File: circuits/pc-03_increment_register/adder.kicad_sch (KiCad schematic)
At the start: 9 parts, among them U10 4081, U11 4070, U12 4070, U13 4011, U5 74LS283, U6 74LS283, U7 74LS283, U8 74LS283, U9 4081

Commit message: Kicad upgrade to 9.0
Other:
- company: (none) -> Adder Circuit
- title: (none) -> PC-03 Increment Unit
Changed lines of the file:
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@@
 (kicad_sch
-	(version 20231120)
+	(version 20250114)
 	(generator "eeschema")
-	(generator_version "8.0")
+	(generator_version "9.0")
 	(paper "A4")
+	(title_block
+		(title "PC-03 Increment Unit")
+		(date "2025-02-18")
+		(rev "A")
+		(company "Adder Circuit")
+	)
 	(junction
 		(at 171.45 86.36)
@@
 	(label "reg9"
 		(at 120.65 68.58 0)
-		(fields_autoplaced yes)
 		(effects
 			(font
@@
 	(label "reg11"
 		(at 120.65 73.66 0)
-		(fields_autoplaced yes)
 		(effects
 			(font
@@
 	(label "inc14"
 		(at 196.85 66.04 0)
-		(fields_autoplaced yes)
 		(effects
 			(font
@@
 	(label "inc3"
 		(at 59.69 68.58 0)
-		(fields_autoplaced yes)
 		(effects
 			(font
@@
 	(label "inc7"
 		(at 105.41 68.58 0)
-		(fields_autoplaced yes)
 		(effects
 			(font
@@
 	(label "reg6"
 		(at 74.93 71.12 0)
-		(fields_autoplaced yes)
 		(effects
 			(font
@@
 	(label "inc15"
 		(at 196.85 68.58 0)
-		(fields_autoplaced yes)
 		(effects
 			(font
@@
 	(label "reg3"
 		(at 29.21 73.66 0)
-		(fields_autoplaced yes)
 		(effects
 			(font
@@
 	(label "reg13"
 		(at 166.37 68.58 0)
-		(fields_autoplaced yes)
 		(effects
 			(font
@@
 	(label "reg12"
 		(at 166.37 66.04 0)
-		(fields_autoplaced yes)
 		(effects
 			(font
@@
 	(label "reg4"
 		(at 74.93 66.04 0)
-		(fields_autoplaced yes)
 		(effects
 			(font
@@
 	(label "inc4"
 		(at 105.41 60.96 0)
-		(fields_autoplaced yes)
 		(effects
 			(font
@@
 	(label "reg0"
 		(at 29.21 66.04 0)
-		(fields_autoplaced yes)
 		(effects
 			(font
@@
 	(label "reg14"
 		(at 166.37 71.12 0)
-		(fields_autoplaced yes)
 		(effects
 			(font
@@
 	(label "reg1"
 		(at 29.21 68.58 0)
-		(fields_autoplaced yes)
 		(effects
 			(font
@@
 	(label "offset6"
 		(at 132.08 172.72 0)
-		(fields_autoplaced yes)
 		(effects
 			(font
@@
 	(label "inc11"
 		(at 151.13 68.58 0)
-		(fields_autoplaced yes)
 		(effects
 			(font
@@
 	(label "inc9"
 		(at 151.13 63.5 0)
-		(fields_autoplaced yes)
 		(effects
 			(font
@@
 	(label "inc10"
 		(at 151.13 66.04 0)
-		(fields_autoplaced yes)
 		(effects
 			(font
@@
 	(label "inc8"
 		(at 151.13 60.96 0)
-		(fields_autoplaced yes)
 		(effects
 			(font
@@
 	(label "inc12"
 		(at 196.85 60.96 0)
-		(fields_autoplaced yes)
 		(effects
 			(font
@@
 	(label "inc0"
 		(at 59.69 60.96 0)
-		(fields_autoplaced yes)
 		(effects
 			(font
@@
 	(label "reg5"
 		(at 74.93 68.58 0)
-		(fields_autoplaced yes)
 		(effects
 			(font
@@
 	(label "inc6"
 		(at 105.41 66.04 0)
-		(fields_autoplaced yes)
 		(effects
 			(font
@@
 	(label "reg7"
 		(at 74.93 73.66 0)
-		(fields_autoplaced yes)
 		(effects
 			(font
@@
 	(label "reg10"
 		(at 120.65 71.12 0)
-		(fields_autoplaced yes)
 		(effects
 			(font
@@
 	(label "offset3"
 		(at 82.55 172.72 0)
-		(fields_autoplaced yes)
 		(effects
 			(font
@@
 	(label "offset4"
 		(at 101.6 172.72 0)
-		(fields_autoplaced yes)
 		(effects
 			(font
@@
 	(label "offset2"
 		(at 67.31 172.72 0)
-		(fields_autoplaced yes)
 		(effects
 			(font
@@
 	(label "inc13"
 		(at 196.85 63.5 0)
-		(fields_autoplaced yes)
 		(effects
 			(font
@@
 	(label "offset1"
 		(at 52.07 172.72 0)
-		(fields_autoplaced yes)
 		(effects
 			(font
@@
 	(label "inc1"
 		(at 59.69 63.5 0)
-		(fields_autoplaced yes)
 		(effects
 			(font
@@
 	(label "offset5"
 		(at 116.84 172.72 0)
-		(fields_autoplaced yes)
 		(effects
 			(font
@@
 	(label "offset0"
 		(at 36.83 172.72 0)
-		(fields_autoplaced yes)
 		(effects
 			(font
@@
 	(label "offset7"
 		(at 147.32 172.72 0)
-		(fields_autoplaced yes)
 		(effects
 			(font
@@
 	(label "inc2"
 		(at 59.69 66.04 0)
-		(fields_autoplaced yes)
 		(effects
 			(font
@@
 	(label "carry_in"
 		(at 187.96 102.87 0)
-		(fields_autoplaced yes)
 		(effects
 			(font
@@
 	(label "reg2"
 		(at 29.21 71.12 0)
-		(fields_autoplaced yes)
 		(effects
 			(font
@@
 	(label "inc5"
 		(at 105.41 63.5 0)
-		(fields_autoplaced yes)
 		(effects
 			(font
@@
 	(label "reg8"
 		(at 120.65 66.04 0)
-		(fields_autoplaced yes)
 		(effects
 			(font
@@
 	(label "reg15"
 		(at 166.37 73.66 0)
-		(fields_autoplaced yes)
 		(effects
 			(font
@@
 		(shape output)
 		(at 204.47 52.07 90)
-		(fields_autoplaced yes)
 		(effects
 			(font
@@
 		(shape output)
 		(at 158.75 52.07 90)
-		(fields_autoplaced yes)
 		(effects
 			(font
@@
 		(shape input)
 		(at 118.11 59.69 90)
-		(fields_autoplaced yes)
 		(effects
 			(font
@@
 		(shape output)
 		(at 67.31 52.07 90)
-		(fields_autoplaced yes)
 		(effects
 			(font
@@
 		(shape input)
 		(at 72.39 59.69 90)
-		(fields_autoplaced yes)
 		(effects
 			(font
@@
 		(shape output)
 		(at 113.03 52.07 90)
-		(fields_autoplaced yes)
 		(effects
 			(font
@@
 		(shape input)
 		(at 25.4 149.86 180)
-		(fields_autoplaced yes)
 		(effects
 			(font
@@
 		(shape input)
 		(at 25.4 175.26 180)
-		(fields_autoplaced yes)
 		(effects
 			(font
@@
 		(shape input)
 		(at 163.83 59.69 90)
-		(fields_autoplaced yes)
 		(effects
 			(font
@@
 		(shape input)
 		(at 26.67 59.69 90)
-		(fields_autoplaced yes)
 		(effects
 			(font
@@
 		(shape input)
 		(at 25.4 170.18 180)
-		(fields_autoplaced yes)
-		(effects
-			(font
+		(effects
+			(font

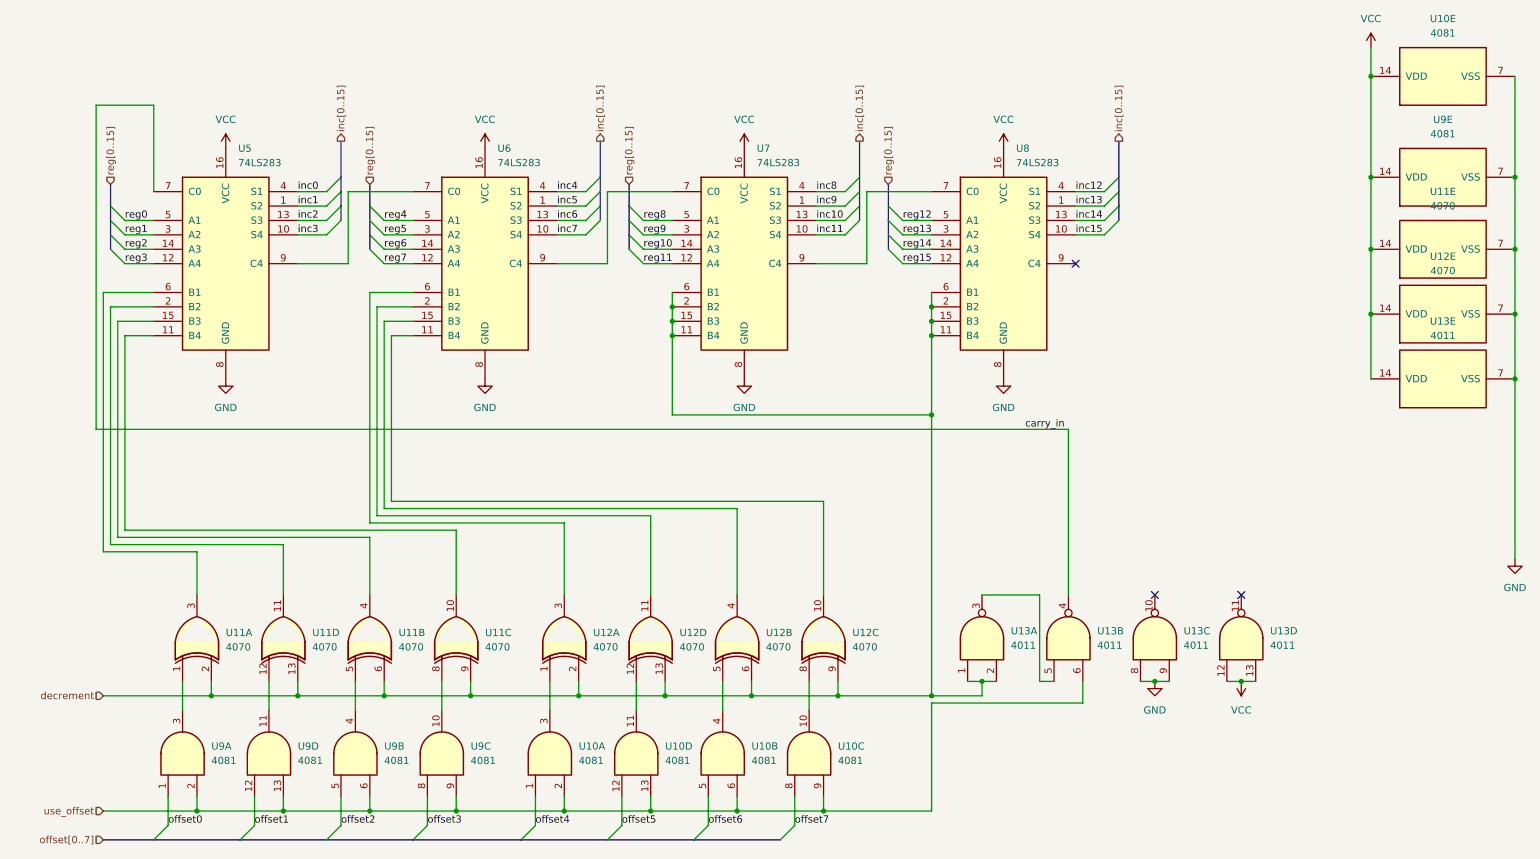
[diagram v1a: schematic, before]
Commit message: PC-03: fix incrementer unit
 * adders are TTL, the weak pull-down on the `inc_dec` signal was not enough to drive the 8 directly connected adder pins correctly. Fixed through the introduction of a non-inverting buffer on that signal to produce hard signals in both directions.
 * incorrect logic caused decrement mode (INCR-1) to calculate (INCR-1+1) by mistake. reworked logic by replacing the old CD4011 NAND by a CD4070 XOR.
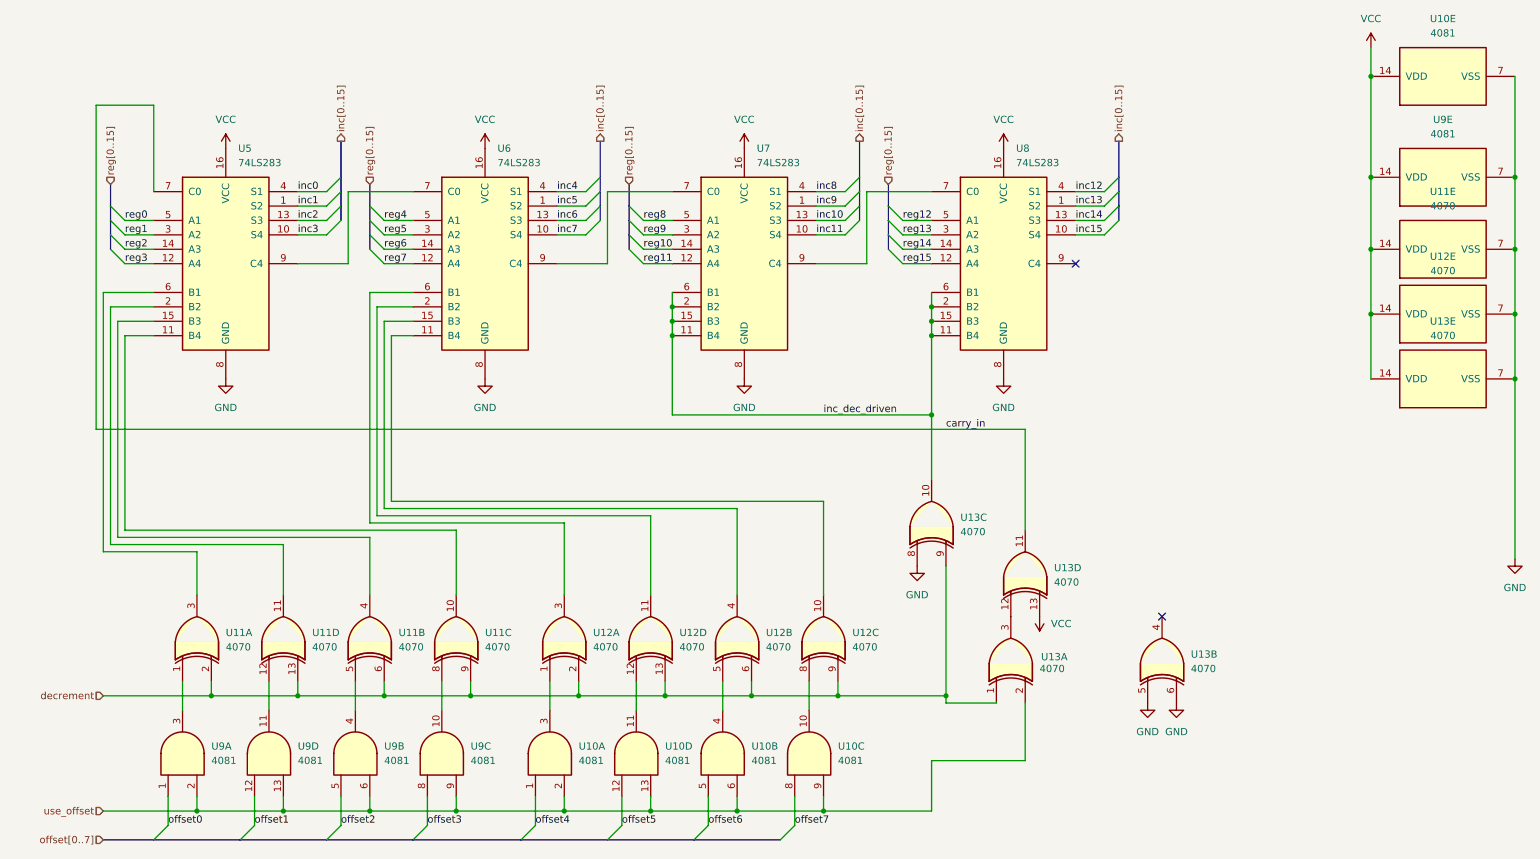
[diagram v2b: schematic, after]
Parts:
- removed U13: 4011, Package_DIP:DIP-14_W7.62mm_LongPads, symbol 4xxx:4011
- added U13: 4070, Package_DIP:DIP-14_W7.62mm_LongPads, symbol 4xxx:4070
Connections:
- net GND: now also U13.5, U13.6, U13.7 (VSS), U13.8
- net VCC: now also U13.13, U13.14 (VDD)
- net carry_in: now also U13.11
- net decrement: now also U13.1, U13.9; no longer U7.11 (B4), U7.15 (B3), U7.2 (B2), U7.6 (B1), U8.11 (B4), U8.15 (B3), U8.2 (B2), U8.6 (B1)
- net use_offset: now also U13.2
- new net: U13.12, U13.3
- new net inc_dec_driven: U13.10, U7.11 (B4), U7.15 (B3), U7.2 (B2), U7.6 (B1), U8.11 (B4), U8.15 (B3), U8.2 (B2), U8.6 (B1)
- no-connect marks 3 -> 2

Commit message: pc-03: add double buffering to incrementer unit
This ensures stable data from the incrementer.
Previously, the published address would change at the start of the write cycle.
With the double buffering introduced, the current value of the address bus is latched into the first register at the start of the write cycle and pushed to the second register at the end of the write cycle.
This way the latched address is only seen by the incrementer at the start of the next cycle, ensuring a stable address bus state during the entire program step.
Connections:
- net GND: no longer U13.5, U13.6
- net VCC: now also U13.6
- net sec_6: now reaches U12.4, U6.15 (B3)
- net sec_3: now reaches U11.10, U5.11 (B4)
- net ~{carry_in}: now reaches U13.12, U13.3
- net sec_7: now reaches U12.10, U6.11 (B4)
- net sec_2: now reaches U11.4, U5.15 (B3)
- net sec_0: now reaches U11.3, U5.6 (B1)
- net c12: now reaches U7.9 (C4), U8.7 (C0)
- net sec_1: now reaches U11.11, U5.2 (B2)
- net c4: now reaches U5.9 (C4), U6.7 (C0)
- net c8: now reaches U6.9 (C4), U7.7 (C0)
- net ~{clock}: now reaches U13.4
- net sec_5: now reaches U12.11, U6.2 (B2)
- net sec_4: now reaches U12.3, U6.6 (B1)
- net inc_dec_driven renamed dec_TTL
- new net clock: U13.5
- no-connect marks 2 -> 1
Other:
- note added: "clock inverter for double buffering"
- moved on the sheet: U13A, U13B, U13D
